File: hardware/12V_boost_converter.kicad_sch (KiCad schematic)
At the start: 23 parts, among them Q201 AO3401A, U201 TPS65131RGE

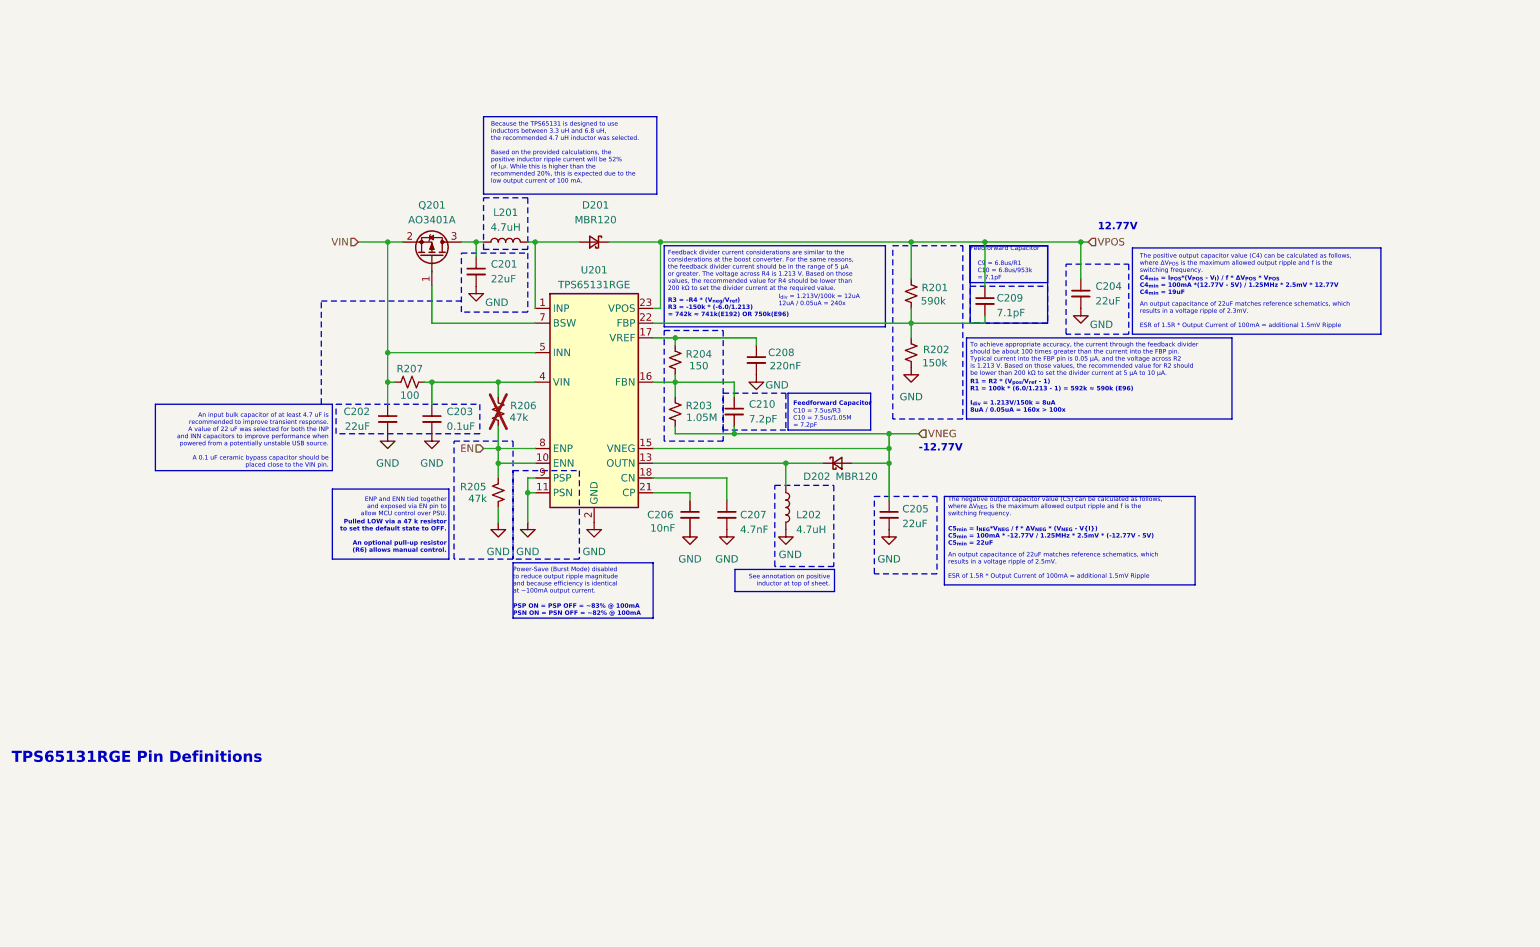
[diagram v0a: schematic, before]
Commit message: Complete 12V rail supply
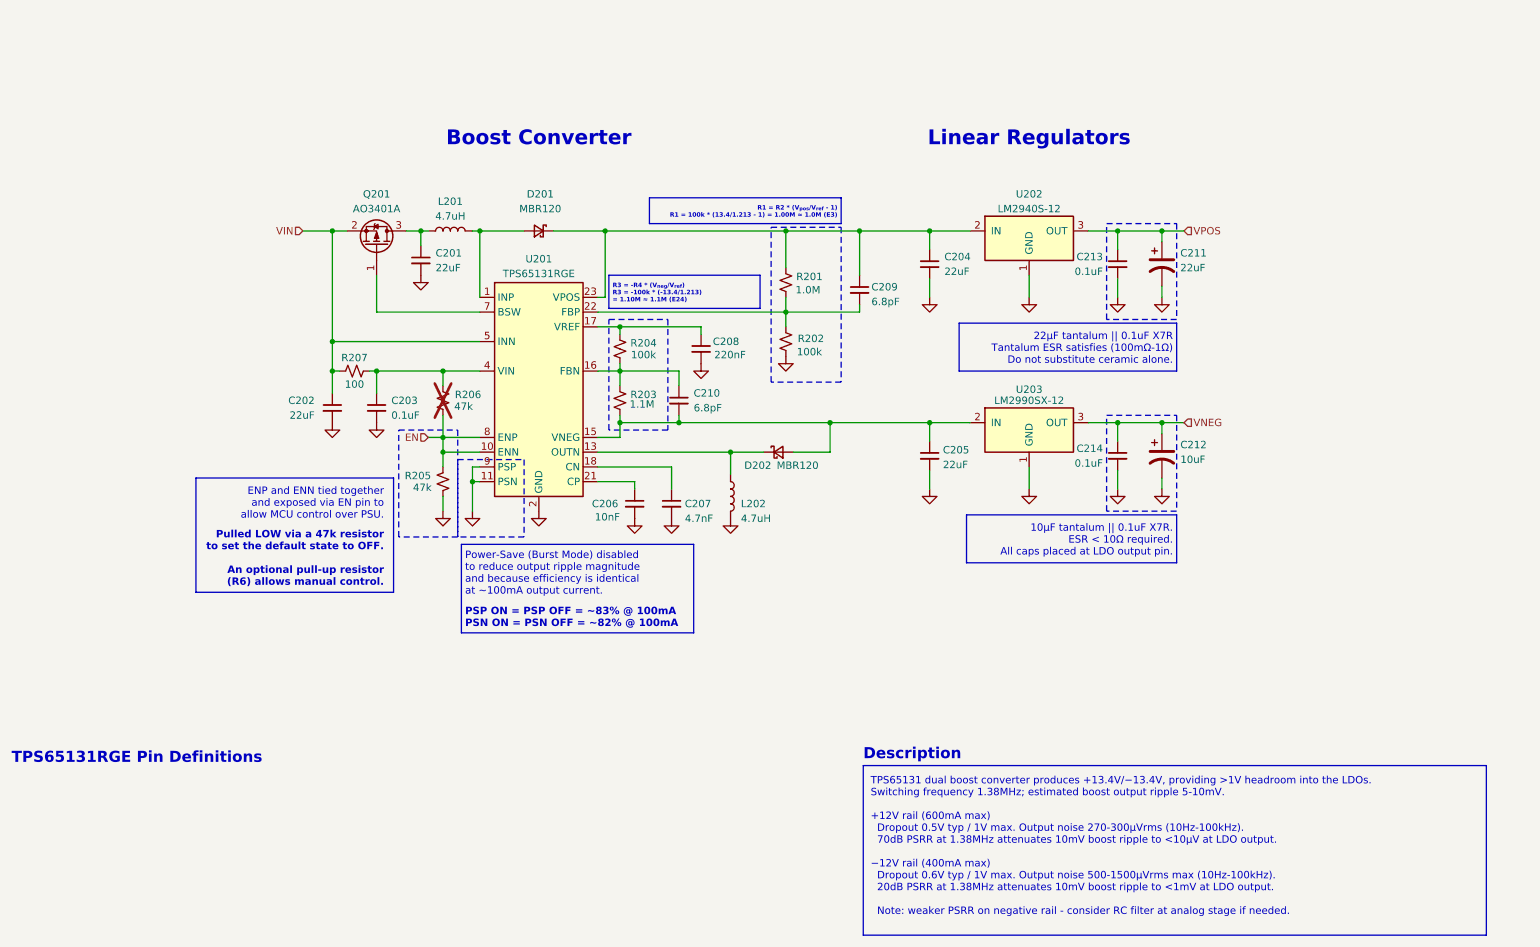
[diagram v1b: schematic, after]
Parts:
- added C211: 22uF, symbol Device:C_Polarized_US
- added C212: 10uF, symbol Device:C_Polarized_US
- added C213, C214: 0.1uF, symbol Device:C_Small
- added U202: LM2940S-12, Package_TO_SOT_SMD:TO-263-3_TabPin2, symbol Regulator_Linear:LM2990SX-12
- added U203: LM2990SX-12, Package_TO_SOT_SMD:TO-263-3_TabPin2, symbol Regulator_Linear:LM2990SX-12
- C209: value 7.1pF -> 6.8pF
- C210: value 7.2pF -> 6.8pF
- R201: value 590k -> 1.0M
- R202: value 150k -> 100k
- R203: value 1.05M -> 1.1M
- R204: value 150 -> 100k
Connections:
- net GND: now also C211.2, C212.2, C213.2, C214.2, U202.1 (GND), U203.1 (GND)
- net VNEG: now also C212.1, C214.1, U203.3 (OUT); no longer C205.1, C210.2, D202.2 (A), R203.1, U201.15 (VNEG)
- net VPOS: now also C211.1, C213.1, U202.3 (OUT); no longer C204.1, C209.1, D201.1 (K), R201.2, U201.23 (VPOS)
- new net: C204.1, C209.1, D201.1 (K), R201.2, U201.23 (VPOS), U202.2 (IN)
- new net: C205.1, C210.2, D202.2 (A), R203.1, U201.15 (VNEG), U203.2 (IN)
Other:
- note added: "10µF tantalum || 0.1uF X7R. ESR < 10Ω required. All caps placed at LDO output pin."
- note added: "22µF tantalum || 0.1uF X7R Tantalum ESR satisfies (100mΩ-1Ω) Do not substitute ceramic alone."
- note added: "Boost Converter"
- note added: "Description"
- note added: "Linear Regulators"
- note added: "Pulled LOW via a 47k resistor to set the default state to OFF. An optional pull-up resistor (R6) allows manual control."
- note added: "R1 = R2 * (V_{pos}/V_{ref} - 1) R1 = 100k * (13.4/1.213 - 1) = 1.00M ≈ 1.0M (E3)"
- note added: "R3 = -R4 * (V_{neg}/V_{ref}) R3 = -100k * (-13.4/1.213) = 1.10M ≈ 1.1M (E24)"
- note added: "TPS65131 dual boost converter produces +13.4V/−13.4V, providing >1V headroom into the LDOs. Switching frequency 1.38MHz; estimated boost output ripple 5-10mV. +12V rail (600mA max) Dropout 0.5V typ / 1V max. Output noise 270-300µVrms (10Hz-100kHz). 70dB PSRR at 1.38MHz attenuates 10mV boost ripple to <10µV at LDO output. −12V rail (400mA max) Dropout 0.6V typ / 1V max. Output noise 500-1500µVrms 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"
- note removed: "-12.77V"
- note removed: "12.77V"
- note removed: "An input bulk capacitor of at least 4.7 uF is recommended to improve transient response. A value of 22 uF was selected for both the INP and INN capacitors to improve performance when powered from a potentially unstable USB source. A 0.1 uF ceramic bypass capacitor should be placed close to the VIN pin."
- note removed: "An output capacitance of 22uF matches reference schematics, which results in a voltage ripple of 2.3mV. ESR of 1.5R * Output Current of 100mA = additional 1.5mV Ripple"
- note removed: "An output capacitance of 22uF matches reference schematics, which results in a voltage ripple of 2.5mV. ESR of 1.5R * Output Current of 100mA = additional 1.5mV Ripple"
- note removed: "Because the TPS65131 is designed to use inductors between 3.3 uH and 6.8 uH, the recommended 4.7 uH inductor was selected. Based on the provided calculations, the positive inductor ripple current will be 52% of I_{LP}. While this is higher than the recommended 20%, this is expected due to the low output current of 100 mA."
- note removed: "C10 = 7.5us/R3 C10 = 7.5us/1.05M = 7.2pF"
- note removed: "C4_{min} = I_{POS}*(V_{POS} - V_{I}) / f * ΔV_{POS} * V_{POS} C4_{min} = 100mA *(12.77V - 5V) / 1.25MHz * 2.5mV * 12.77V C4_{min} = 19uF"
- note removed: "C5_{min} = I_{NEG}*V_{NEG} / f * ΔV_{NEG} * (V_{NEG} - V{I}) C5_{min} = 100mA * -12.77V / 1.25MHz * 2.5mV * (-12.77V - 5V) C5_{min} = 22uF"
- note removed: "C9 = 6.8us/R1 C10 = 6.8us/953k = 7.1pF"
- note removed: "Feedback divider current considerations are similar to the considerations at the boost converter. For the same reasons, the feedback divider current should be in the range of 5 µA or greater. The voltage across R4 is 1.213 V. Based on those values, the recommended value for R4 should be lower than 200 kΩ to set the divider current at the required value."
- note removed: "Feedforward Capacitor"
- note removed: "I_{div} = 1.213V/100k = 12uA 12uA / 0.05uA = 240x"
- note removed: "Pulled LOW via a 47 k resistor to set the default state to OFF. An optional pull-up resistor (R6) allows manual control."
- note removed: "R1 = R2 * (V_{pos}/V_{ref} - 1) R1 = 100k * (6.0/1.213 - 1) = 592k ≈ 590k (E96) I_{div} = 1.213V/150k = 8uA 8uA / 0.05uA = 160x > 100x"
- note removed: "R3 = -R4 * (V_{neg}/V_{ref}) R3 = -150k * (-6.0/1.213) = 742k ≈ 741k(E192) OR 750k(E96)"
- note removed: "See annotation on positive inductor at top of sheet."
- note removed: "The negative output capacitor value (C5) can be calculated as follows, where ΔV_{NEG} is the maximum allowed output ripple and f is the switching frequency."
- note removed: "The positive output capacitor value (C4) can be calculated as follows, where ΔV_{POS} is the maximum allowed output ripple and f is the switching frequency."
- note removed: "To achieve appropriate accuracy, the current through the feedback divider should be about 100 times greater than the current into the FBP pin. Typical current into the FBP pin is 0.05 µA, and the voltage across R2 is 1.213 V. Based on those values, the recommended value for R2 should be lower than 200 kΩ to set the divider current at 5 µA to 10 µA."
- title: Dual Rail Boost Converter -> ±12V Rail Boost Converter & Regulators
- moved on the sheet: C201, C202, C203, C204, C205, C206, C207, C208, C209, C210, D201, D202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

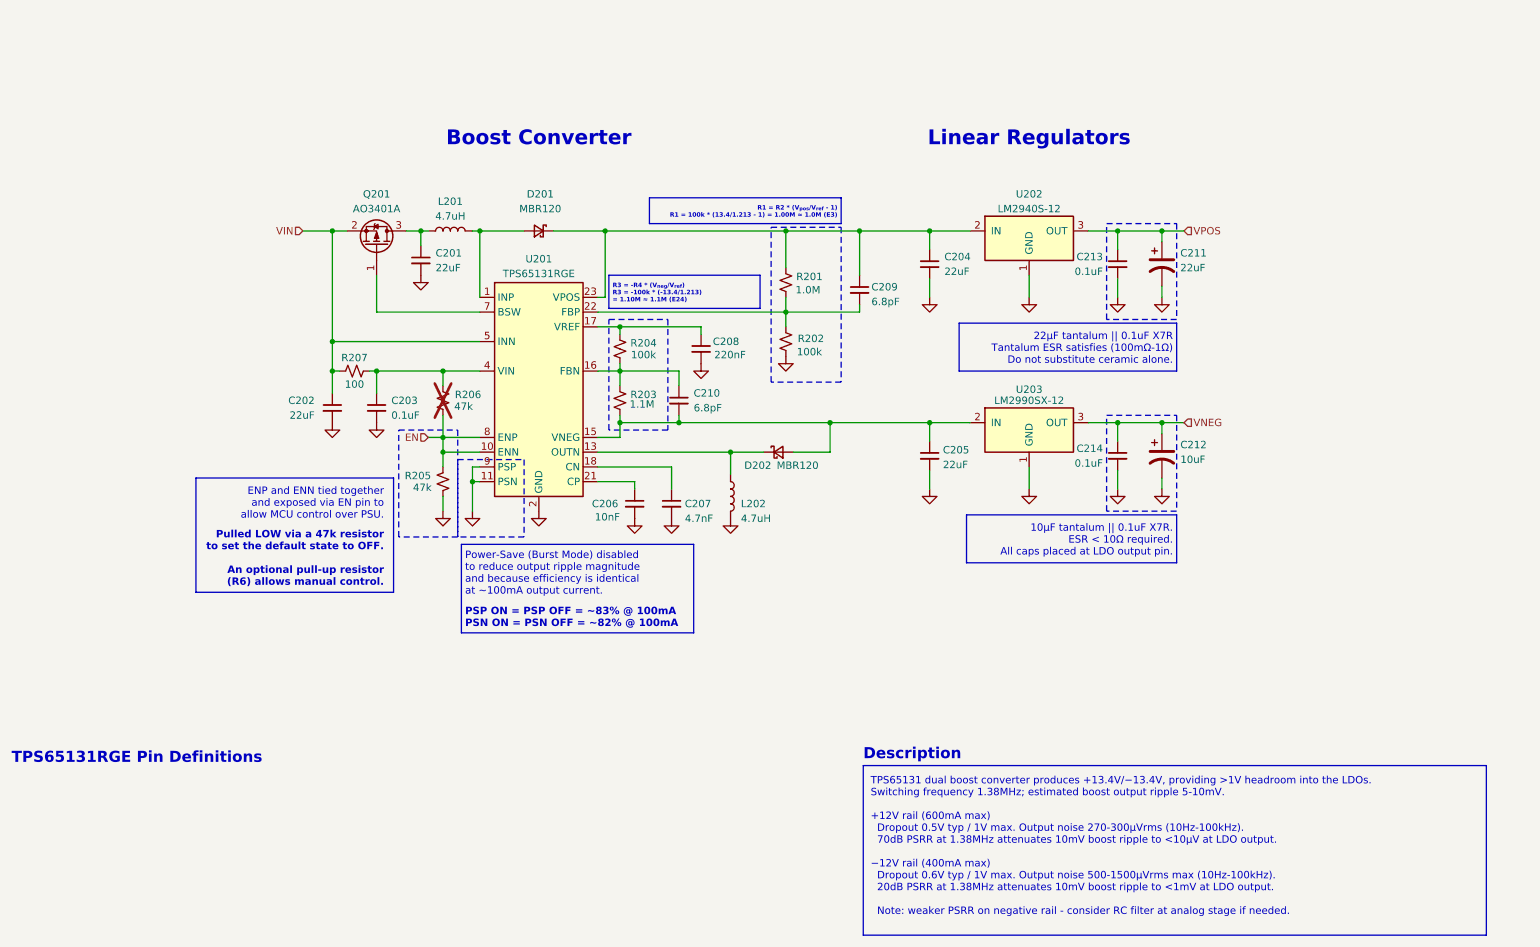
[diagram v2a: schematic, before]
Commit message: Implement TPS7A39 and Annotate
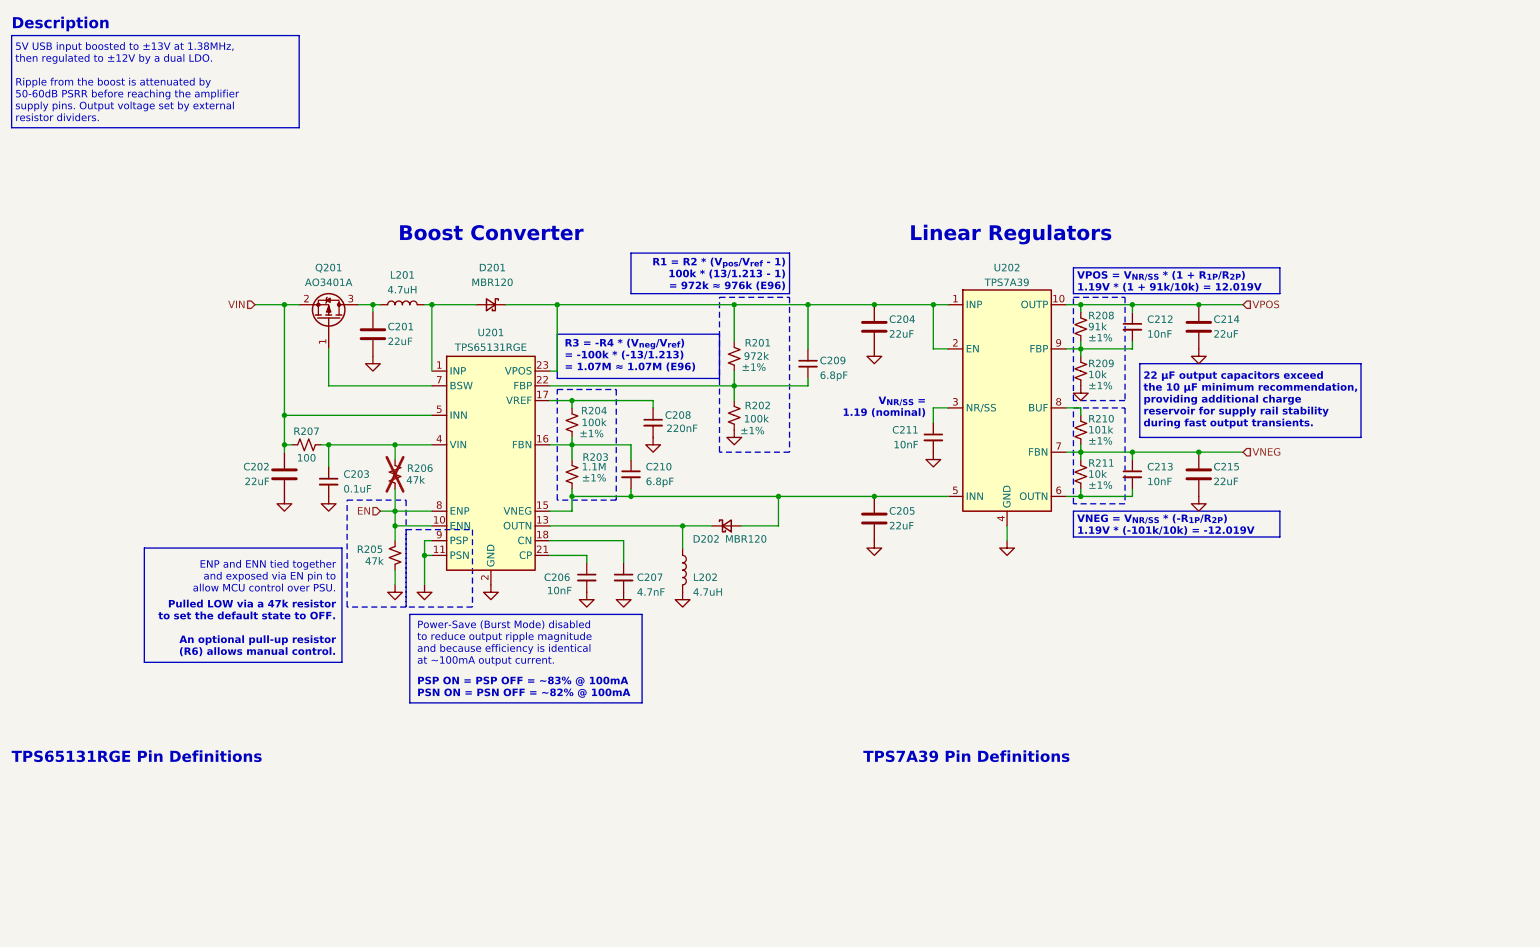
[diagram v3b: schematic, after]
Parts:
- removed C201, C202, C204, C205: 22uF, symbol Device:C_Small
- removed C211: 22uF, symbol Device:C_Polarized_US
- removed C212: 10uF, symbol Device:C_Polarized_US
- removed C214: 0.1uF, symbol Device:C_Small
- removed U202: LM2940S-12, Package_TO_SOT_SMD:TO-263-3_TabPin2, symbol Regulator_Linear:LM2990SX-12
- removed U203: LM2990SX-12, Package_TO_SOT_SMD:TO-263-3_TabPin2, symbol Regulator_Linear:LM2990SX-12
- added C201, C202, C204, C205, C214, C215: 22uF, symbol Device:C
- added C211, C212: 10nF, symbol Device:C_Small
- added R208: 91k, symbol Device:R_Small_US
- added R209, R211: 10k, symbol Device:R_Small_US
- added R210: 101k, symbol Device:R_Small_US
- added U202: TPS7A39, Package_SON:Texas_S-PVSON-N10_ThermalVias, symbol Regulator_Linear:TPS7A39
- C213: value 0.1uF -> 10nF
- R201: value 1.0M -> 972k; Tolerance (none) -> ±1%
- R202, R203, R204: Tolerance (none) -> ±1%
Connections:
- net GND: now also C201.2, C202.2, C204.2, C205.2, C211.2, C214.2, C215.2, R209.2, U202.11 (GND), U202.4 (GND); no longer C213.2
- net VIN: now also C202.1
- net VNEG: now also C213.1, C215.1, R210.2, R211.1, U202.7 (FBN)
- net VPOS: now also C212.1, C214.1, R208.1, U202.10 (OUTP); no longer C213.1
- net at L201.1, Q201.3 (D): now also C201.1
- net at C209.1, D201.1 (K), R201.2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: now also C204.1, U202.1 (INP), U202.2 (EN)
- net at C210.2, D202.2 (A), R203.1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: now also C205.1, U202.5 (INN)
- new net: C212.2, R208.2, R209.1, U202.9 (FBP)
- new net: C213.2, R211.2, U202.6 (OUTN)
- new net: C211.1, U202.3 (NR/SS)
- new net: R210.1, U202.8 (BUF)
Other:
- note added: "22 µF output capacitors exceed the 10 µF minimum recommendation, providing additional charge reservoir for supply rail stability during fast output transients."
- note added: "5V USB input boosted to ±13V at 1.38MHz, then regulated to ±12V by a dual LDO. Ripple from the boost is attenuated by 50-60dB PSRR before reaching the amplifier supply pins. Output voltage set by external resistor dividers."
- note added: "R1 = R2 * (V_{pos}/V_{ref} - 1) 100k * (13/1.213 - 1) = 972k ≈ 976k (E96)"
- note added: "R3 = -R4 * (V_{neg}/V_{ref}) = -100k * (-13/1.213) = 1.07M ≈ 1.07M (E96)"
- note added: "TPS7A39 Pin Definitions"
- note added: "VNEG = V_{NR/SS} * (-R_{1P}/R_{2P}) 1.19V * (-101k/10k) = -12.019V"
- note added: "VPOS = V_{NR/SS} * (1 + R_{1P}/R_{2P}) 1.19V * (1 + 91k/10k) = 12.019V"
- note added: "V_{NR/SS} = 1.19 (nominal)"
- note removed: "10µF tantalum || 0.1uF X7R. ESR < 10Ω required. All caps placed at LDO output pin."
- note removed: "22µF tantalum || 0.1uF X7R Tantalum ESR satisfies (100mΩ-1Ω) Do not substitute ceramic alone."
- note removed: "R1 = R2 * (V_{pos}/V_{ref} - 1) R1 = 100k * (13.4/1.213 - 1) = 1.00M ≈ 1.0M (E3)"
- note removed: "R3 = -R4 * (V_{neg}/V_{ref}) R3 = -100k * (-13.4/1.213) = 1.10M ≈ 1.1M (E24)"
- note removed: "TPS65131 dual boost converter produces +13.4V/−13.4V, providing >1V headroom into the LDOs. Switching frequency 1.38MHz; estimated boost output ripple 5-10mV. +12V rail (600mA max) Dropout 0.5V typ / 1V max. Output noise 270-300µVrms (10Hz-100kHz). 70dB PSRR at 1.38MHz attenuates 10mV boost ripple to <10µV at LDO output. −12V rail (400mA max) Dropout 0.6V typ / 1V max. Output noise 500-1500µVrms 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"
- moved on the sheet: C203, C206, C207, C208, C209, C210, D201, D202, L201, L202, Q201, R201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

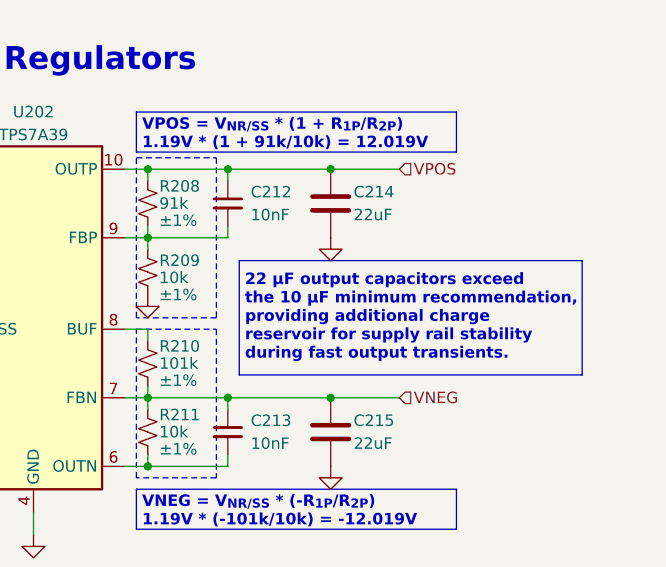
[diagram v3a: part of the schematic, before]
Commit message: Add USB sheet and remove old components
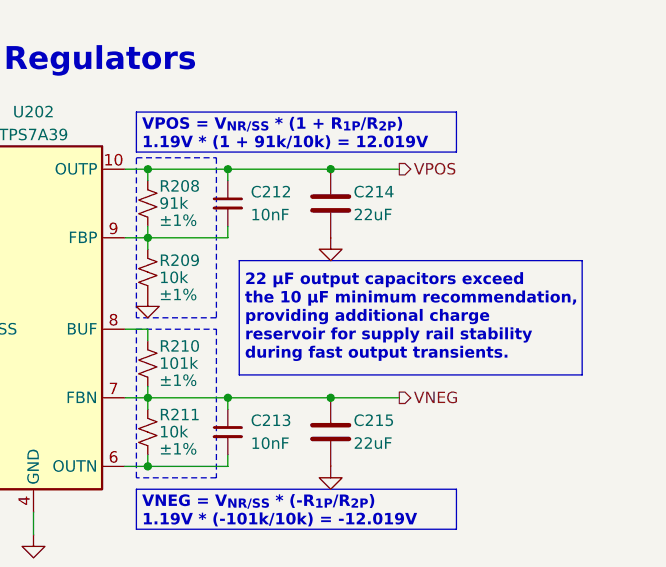
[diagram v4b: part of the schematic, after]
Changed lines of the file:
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@@
 	(title_block
 		(title "±12V Rail Boost Converter & Regulators")
-		(date "2026-04-09")
+		(date "2026-04-11")
 		(rev "A")
 		(company "Jacob Wigent")
@@
 	)
 	(hierarchical_label "VNEG"
-		(shape input)
+		(shape output)
 		(at 224.79 88.265 0)
 		(effects
@@
 	)
 	(hierarchical_label "VPOS"
-		(shape input)
+		(shape output)
 		(at 224.79 62.865 0)
 		(effects
